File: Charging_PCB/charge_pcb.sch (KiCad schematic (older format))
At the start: 35 parts, among them J1 PCB_1, J2 Battery, J3 Power Switch, J4 24V Out, J5 Motor_Left, J6 Motor_Cutter, J7 Motor_Right, Q1 BC547C, Q2 IRLB 8721, Q3 BC547C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

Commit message: PCB Changes
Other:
- moved on the sheet: D1
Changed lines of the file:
@@
 	2500 2250 2500 2400
 Wire Wire Line
-	1550 2250 1650 2250
+	1550 2250 1600 2250
 Wire Wire Line
 	2500 2700 2500 2900
@@
 	6500 3050 6550 3050
 Connection ~ 6500 2400
-Connection ~ 1550 2250
-Connection ~ 1550 3700
-Wire Wire Line
-	1550 3700 650  3700
-Wire Wire Line
-	1550 3700 2000 3700
 Text GLabel 2250 3900 0    50   Output ~ 0
 pinChargeVoltage
 Wire Wire Line
-	1550 3200 1550 3700
-Wire Wire Line
-	1550 2250 1550 2900
+	1600 3200 1600 3700
+Wire Wire Line
+	1600 2250 1600 2900
 $Comp
 L Diode:MBR745 D1
 U 1 1 60702097
-P 1550 3050
-F 0 "D1" V 1504 3130 50  0000 L CNN
-F 1 "MBR1045" V 1595 3130 50  0000 L CNN
-F 2 "Package_TO_SOT_THT:TO-220-2_Vertical" H 1550 2875 50  0001 C CNN
-F 3 "http://www.onsemi.com/pub_link/Collateral/MBR735-D.PDF" H 1550 3050 50  0001 C CNN
-	1    1550 3050
+P 1600 3050
+F 0 "D1" V 1554 3130 50  0000 L CNN
+F 1 "MBR1045" V 1645 3130 50  0000 L CNN
+F 2 "Package_TO_SOT_THT:TO-220-2_Vertical" H 1600 2875 50  0001 C CNN
+F 3 "http://www.onsemi.com/pub_link/Collateral/MBR735-D.PDF" H 1600 3050 50  0001 C CNN
+	1    1600 3050
 	0    1    1    0
 $EndComp
@@
 Wire Wire Line
 	2250 2900 2500 2900
-Connection ~ 1650 2250
-Wire Wire Line
-	1650 2250 1800 2250
 Wire Wire Line
 	2050 2250 2150 2250
@@
 	1    0    0    -1
 $EndComp
+Connection ~ 1600 2250
+Connection ~ 1600 3700
+Wire Wire Line
+	1600 3700 2000 3700
+Wire Wire Line
+	650  3700 1600 3700
+Wire Wire Line
+	1600 2250 1650 2250
 $EndSCHEMATC

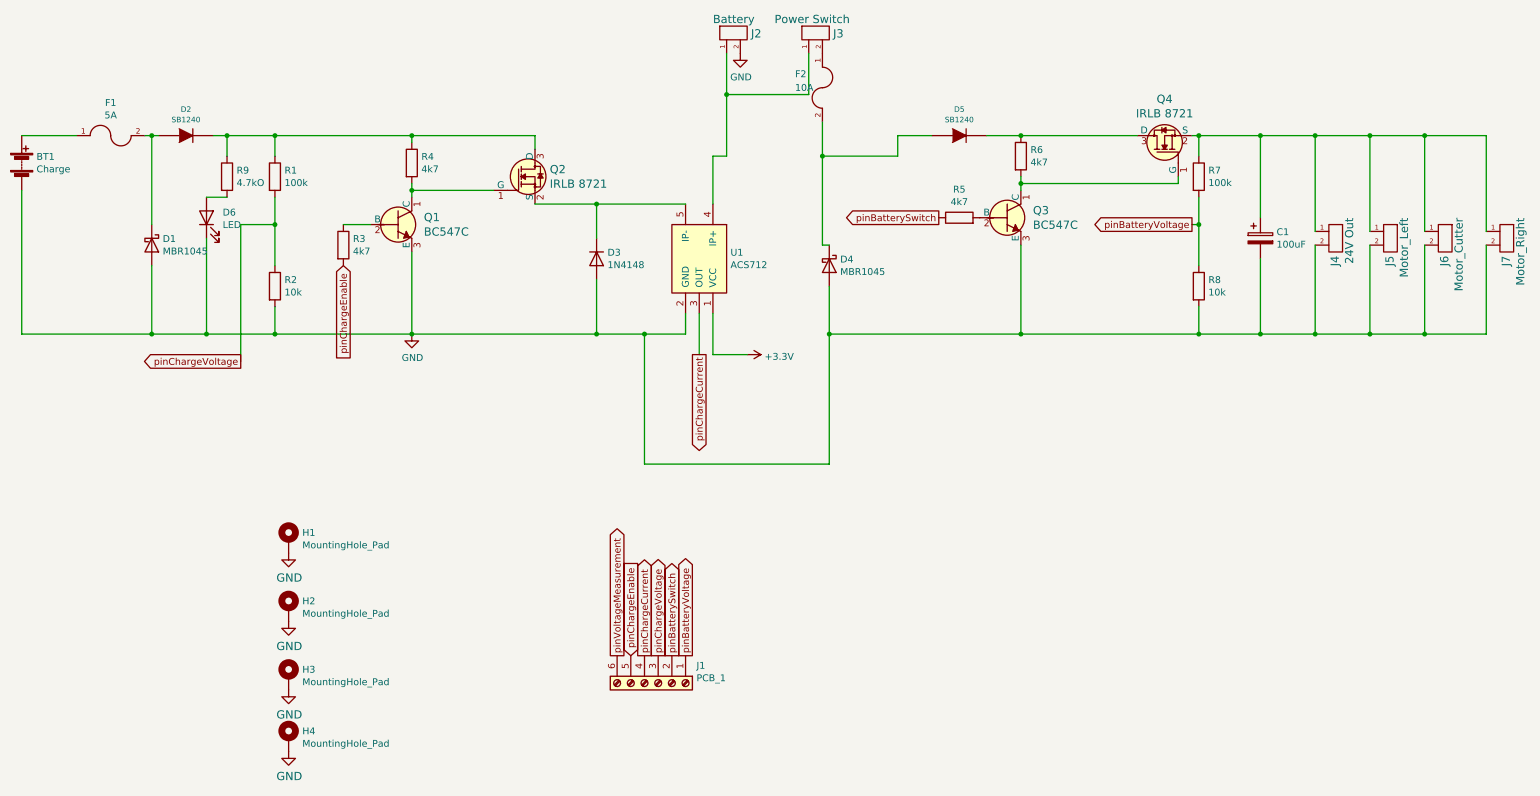
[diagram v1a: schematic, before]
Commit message: Small Changes
Change Q2 & Q4 to IRF9540N
Add Push Button to start the Due
Change pinChargeEnable to pinChargeRelay
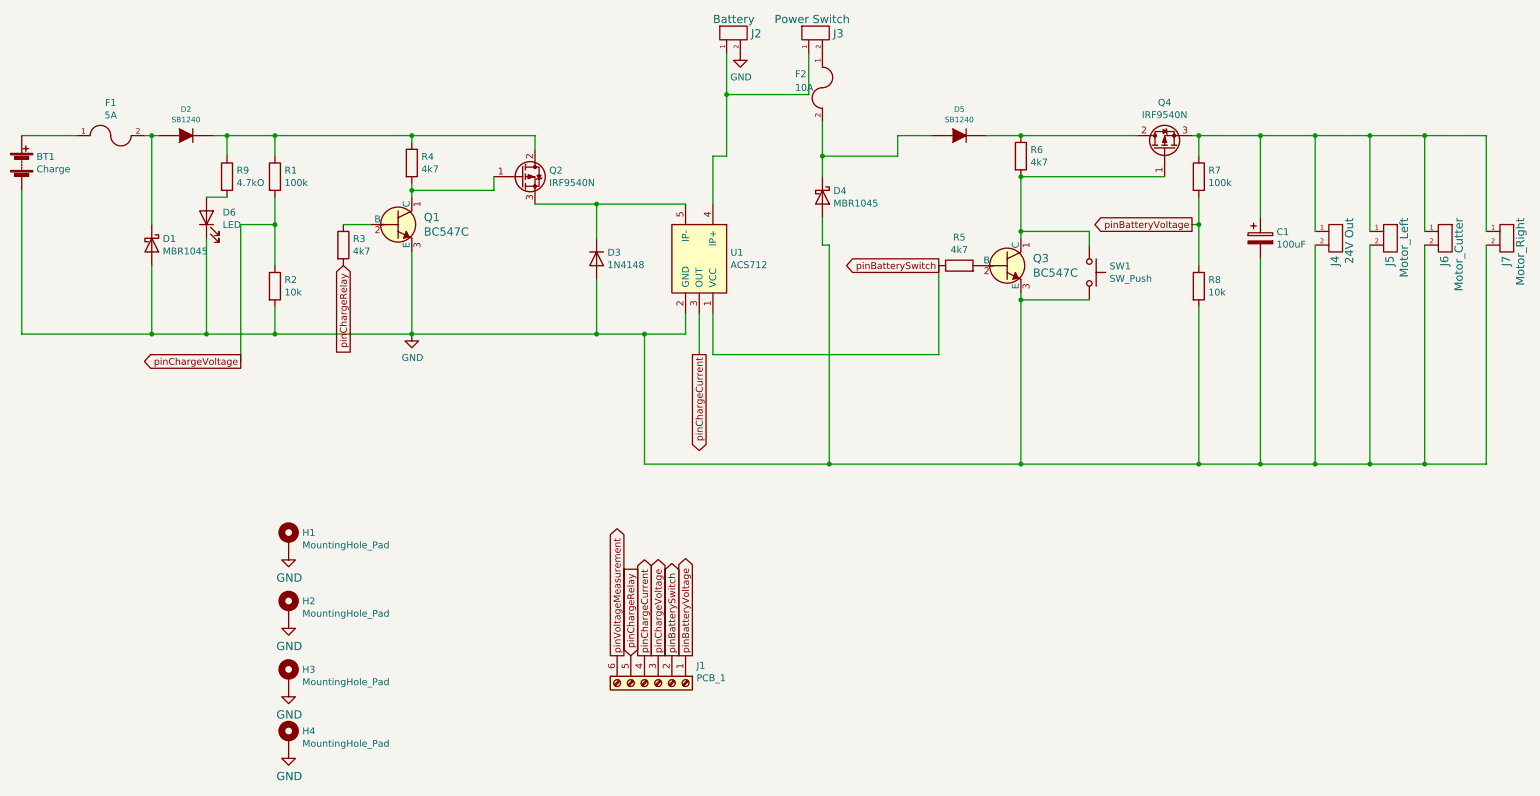
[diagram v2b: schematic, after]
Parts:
- removed Q2, Q4: IRLB 8721, Package_TO_SOT_THT:SIPAK-1EP_Horizontal_TabDown, symbol dk_Transistors-FETs-MOSFETs-Single:IRLML6344TRPBF
- added Q2, Q4: IRF9540N, Package_TO_SOT_THT:TO-220-3_Vertical, symbol Transistor_FET:IRF9540N
- added SW1: SW_Push, Connector_JST:JST_XH_B2B-XH-A_1x02_P2.50mm_Vertical, symbol Switch:SW_Push
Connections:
- net +3V3 is gone; now on net pinBatterySwitch: U1.1 (VCC)
- net GND: now also SW1.2
- net at D2.2 (K), R1.1, R4.1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: now also Q2.2 (D)
- net at Q1.1 (C), R4.2: now also Q2.1 (G)
- net at D3.1 (K), U1.5 (IP-): now also Q2.3 (S)
- net at Q3.1 (C), R6.2: now also Q4.1 (G), SW1.1
- net at C1.1, J4.1, J5.1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: now also Q4.3 (S)
- net at D5.2 (K), R6.1: now also Q4.2 (D)
- net pinChargeEnable renamed pinChargeRelay
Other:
- moved on the sheet: D4, Q3, R5
